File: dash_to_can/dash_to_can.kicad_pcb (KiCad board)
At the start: 2 copper layers, 100 x 100 mm, 64 parts, among them J1 AVR-ISP1, J2 Conn_02x10_Top_Bottom, Q1 2N3904, Q10 AO3401A, Q2 2N3904, Q3 2N3904, Q4 AO3401A, Q5 2N3904, Q6 AO3401A, Q7 2N3904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

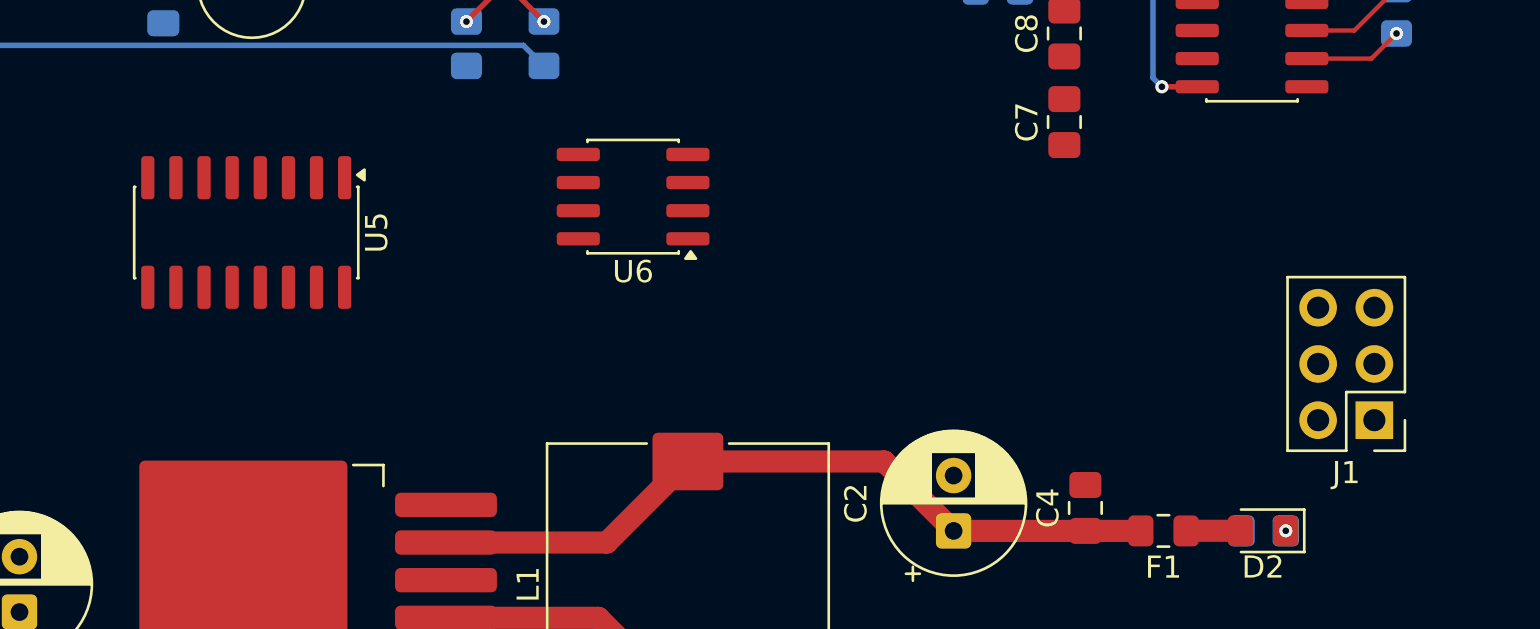
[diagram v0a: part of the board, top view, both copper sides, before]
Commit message: fixing footprint warnings
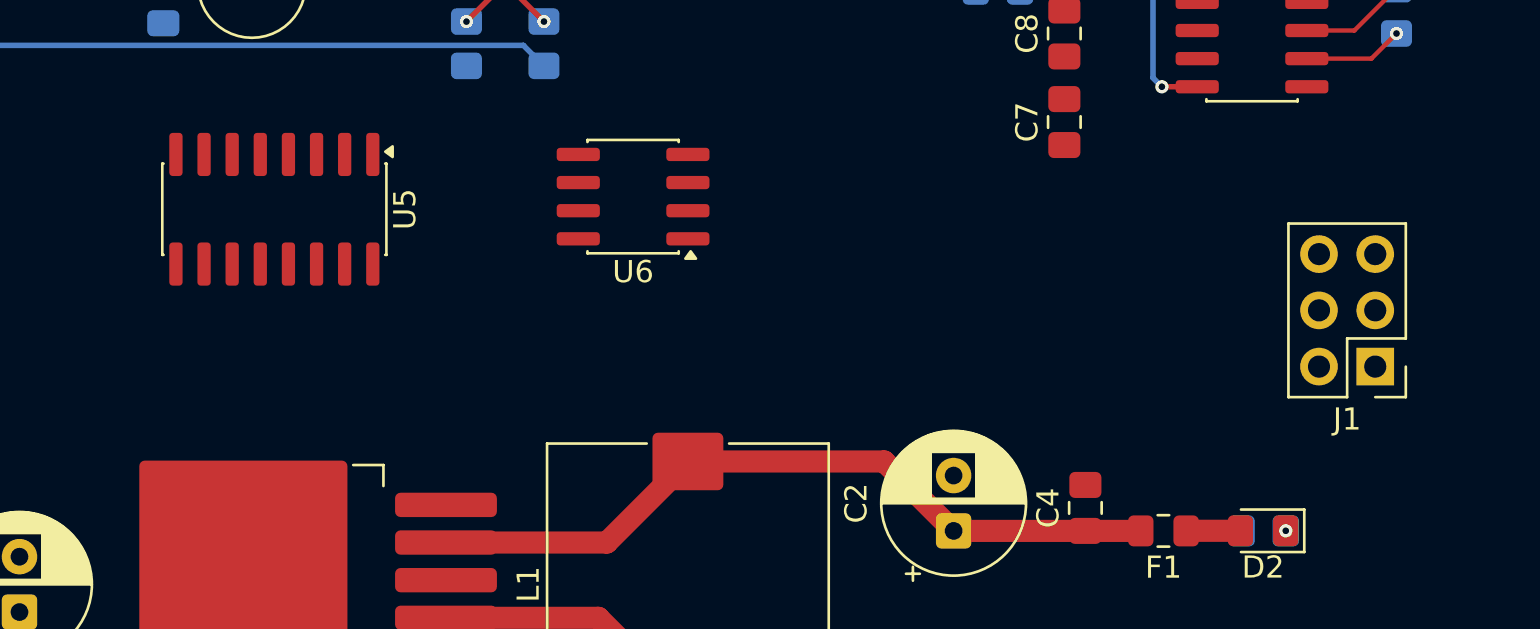
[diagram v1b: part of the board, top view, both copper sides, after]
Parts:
- moved J1 2.42 mm to (154.5, 93.1)
- moved U5 1.65 mm to (104.8, 86.0)
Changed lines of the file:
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@@
 	(footprint "Package_SO:SOIC-16_3.9x9.9mm_P1.27mm"
 		(layer "F.Cu")
-		(at 103.555 87.025 -90)
+		(at 104.825 85.975 -90)
 		(descr "SOIC, 16 Pin (JEDEC MS-012, variation AC, https://www.jedec.org/document_search?search_api_views_fulltext=MS-012, https://www.analog.com/media/en/package-pcb-resources/package/pkg_pdf/soic_narrow-r/r_16.pdf), generated with kicad-footprint-generator ipc_gullwing_generator.py")
 		(tags "SOIC SO 16-pin-NSOP R-16 R-16-S D0016A M2B SO16 SOT109-1 751B SOIC_N narrow")
@@
 	(footprint "Connector_PinHeader_2.54mm:PinHeader_2x03_P2.54mm_Vertical"
 		(layer "F.Cu")
-		(at 154.5 95.5 180)
+		(at 154.54 93.08 180)
 		(descr "Through hole straight pin header, 2x03, 2.54mm pitch, double rows")
 		(tags "Through hole pin header THT 2x03 2.54mm double row")
